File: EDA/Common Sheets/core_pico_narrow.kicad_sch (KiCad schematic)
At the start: 15 parts, among them J6 Conn_01x02, SW1 SW_DIP_x03, U1 Pico(2(W))

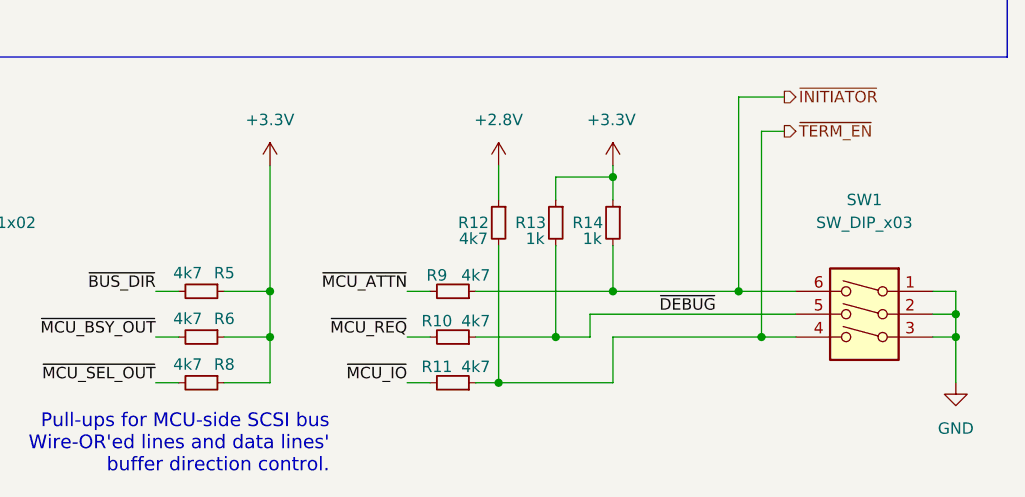
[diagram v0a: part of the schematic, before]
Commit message: Started work on thru-hole SCA wide variant
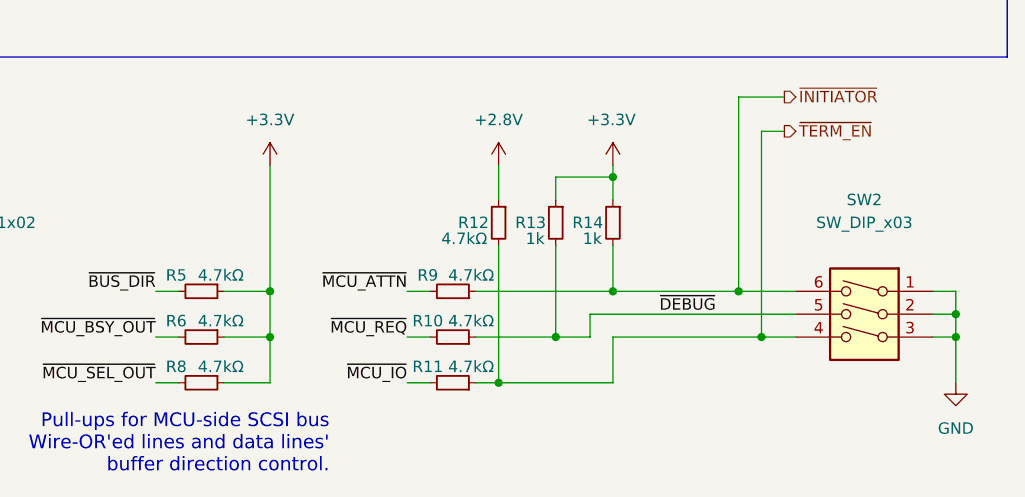
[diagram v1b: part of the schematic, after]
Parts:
- R10, R11, R12, R5, R6, R8, R9: value 4k7 -> 4.7kΩ
- renumbered SW1 to SW2
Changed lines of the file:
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@@
 		(dnp no)
 		(property "Reference" "R10"
-			(at 129.032 176.022 90)
-			(effects
-				(font
-					(size 1.27 1.27)
-				)
-			)
-		)
-		(property "Value" "4k7"
-			(at 133.35 176.022 90)
+			(at 128.016 176.022 90)
+			(effects
+				(font
+					(size 1.27 1.27)
+				)
+			)
+		)
+		(property "Value" "4.7kΩ"
+			(at 132.842 176.022 90)
 			(effects
 				(font
@@
 		(dnp no)
 		(property "Reference" "R6"
-			(at 105.41 175.768 90)
-			(effects
-				(font
-					(size 1.27 1.27)
-				)
-			)
-		)
-		(property "Value" "4k7"
-			(at 101.346 175.768 90)
+			(at 100.076 176.022 90)
+			(effects
+				(font
+					(size 1.27 1.27)
+				)
+			)
+		)
+		(property "Value" "4.7kΩ"
+			(at 105.029 176.022 90)
 			(effects
 				(font
@@
 		(dnp no)
 		(property "Reference" "R9"
-			(at 129.032 170.942 90)
-			(effects
-				(font
-					(size 1.27 1.27)
-				)
-			)
-		)
-		(property "Value" "4k7"
-			(at 133.35 170.942 90)
+			(at 128.016 170.942 90)
+			(effects
+				(font
+					(size 1.27 1.27)
+				)
+			)
+		)
+		(property "Value" "4.7kΩ"
+			(at 132.842 170.942 90)
 			(effects
 				(font
@@
 		(dnp no)
 		(property "Reference" "R8"
-			(at 105.41 180.848 90)
-			(effects
-				(font
-					(size 1.27 1.27)
-				)
-			)
-		)
-		(property "Value" "4k7"
-			(at 101.346 180.848 90)
+			(at 100.076 181.102 90)
+			(effects
+				(font
+					(size 1.27 1.27)
+				)
+			)
+		)
+		(property "Value" "4.7kΩ"
+			(at 105.029 181.102 90)
 			(effects
 				(font
@@
 		(dnp no)
 		(property "Reference" "R11"
-			(at 129.032 181.102 90)
-			(effects
-				(font
-					(size 1.27 1.27)
-				)
-			)
-		)
-		(property "Value" "4k7"
-			(at 133.35 181.102 90)
+			(at 128.016 181.102 90)
+			(effects
+				(font
+					(size 1.27 1.27)
+				)
+			)
+		)
+		(property "Value" "4.7kΩ"
+			(at 132.842 181.102 90)
 			(effects
 				(font
@@
 		(dnp no)
 		(property "Reference" "R5"
-			(at 105.41 170.688 90)
-			(effects
-				(font
-					(size 1.27 1.27)
-				)
-			)
-		)
-		(property "Value" "4k7"
-			(at 101.346 170.688 90)
+			(at 100.076 170.942 90)
+			(effects
+				(font
+					(size 1.27 1.27)
+				)
+			)
+		)
+		(property "Value" "4.7kΩ"
+			(at 105.029 170.942 90)
 			(effects
 				(font
@@
 			)
 		)
-		(property "Value" "4k7"
-			(at 133.096 166.878 0)
+		(property "Value" "4.7kΩ"
+			(at 132.08 166.878 0)
 			(effects
 				(font
@@
 		(on_board yes)
 		(dnp no)
-		(property "Reference" "SW1"
+		(property "Reference" "SW2"
 			(at 176.53 162.56 0)
 			(effects
@@
 			(project "GBSCSI2_2.5N_Pico"
 				(path "/93ed3756-682c-4bf3-aa83-42c6b59d82c2/871f9ffd-aa9f-4db2-af7f-735335bcb730"
-					(reference "SW1")
-					(unit 1)
-				)
+					(reference "SW2")
+					(unit 1)
+				)

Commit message: Resuming work
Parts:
- U1: footprint GBSCSI:RPi_Pico_W_SMD_TH -> GBSCSI:RPi_Pico_W_SMD
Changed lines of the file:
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@@
 		)
 		(instances
-			(project "GBSCSI2_2.5N_Pico"
+			(project "GBSCSI2_DB25_Pico"
 				(path "/93ed3756-682c-4bf3-aa83-42c6b59d82c2/871f9ffd-aa9f-4db2-af7f-735335bcb730"
 					(reference "D5")
@@
 		)
 		(instances
-			(project "GBSCSI2_2.5N_Pico"
+			(project "GBSCSI2_DB25_Pico"
 				(path "/93ed3756-682c-4bf3-aa83-42c6b59d82c2/871f9ffd-aa9f-4db2-af7f-735335bcb730"
 					(reference "R10")
@@
 		)
 		(instances
-			(project "GBSCSI2_2.5N_Pico"
+			(project "GBSCSI2_DB25_Pico"
 				(path "/93ed3756-682c-4bf3-aa83-42c6b59d82c2/871f9ffd-aa9f-4db2-af7f-735335bcb730"
 					(reference "#PWR02")
@@
 		)
 		(instances
-			(project "GBSCSI2_2.5N_Pico"
+			(project "GBSCSI2_DB25_Pico"
 				(path "/93ed3756-682c-4bf3-aa83-42c6b59d82c2/871f9ffd-aa9f-4db2-af7f-735335bcb730"
 					(reference "#PWR021")
@@
 		)
 		(instances
-			(project "GBSCSI2_2.5N_Pico"
+			(project "GBSCSI2_DB25_Pico"
 				(path "/93ed3756-682c-4bf3-aa83-42c6b59d82c2/871f9ffd-aa9f-4db2-af7f-735335bcb730"
 					(reference "#PWR03")
@@
 		)
 		(instances
-			(project "GBSCSI2_2.5N_Pico"
+			(project "GBSCSI2_DB25_Pico"
 				(path "/93ed3756-682c-4bf3-aa83-42c6b59d82c2/871f9ffd-aa9f-4db2-af7f-735335bcb730"
 					(reference "#PWR023")
@@
 		)
 		(instances
-			(project "GBSCSI2_2.5N_Pico"
+			(project "GBSCSI2_DB25_Pico"
 				(path "/93ed3756-682c-4bf3-aa83-42c6b59d82c2/871f9ffd-aa9f-4db2-af7f-735335bcb730"
 					(reference "R6")
@@
 		)
 		(instances
-			(project "GBSCSI2_2.5N_Pico"
+			(project "GBSCSI2_DB25_Pico"
 				(path "/93ed3756-682c-4bf3-aa83-42c6b59d82c2/871f9ffd-aa9f-4db2-af7f-735335bcb730"
 					(reference "R55")
@@
 		)
 		(instances
-			(project "GBSCSI2_2.5N_Pico"
+			(project "GBSCSI2_DB25_Pico"
 				(path "/93ed3756-682c-4bf3-aa83-42c6b59d82c2/871f9ffd-aa9f-4db2-af7f-735335bcb730"
 					(reference "R9")
@@
 		)
 		(instances
-			(project "GBSCSI2_2.5N_Pico"
+			(project "GBSCSI2_DB25_Pico"
 				(path "/93ed3756-682c-4bf3-aa83-42c6b59d82c2/871f9ffd-aa9f-4db2-af7f-735335bcb730"
 					(reference "#PWR04")
@@
 		)
 		(instances
-			(project "GBSCSI2_2.5N_Pico"
+			(project "GBSCSI2_DB25_Pico"
 				(path "/93ed3756-682c-4bf3-aa83-42c6b59d82c2/871f9ffd-aa9f-4db2-af7f-735335bcb730"
 					(reference "#PWR017")
@@
 		)
 		(instances
-			(project "GBSCSI2_2.5N_Pico"
+			(project "GBSCSI2_DB25_Pico"
 				(path "/93ed3756-682c-4bf3-aa83-42c6b59d82c2/871f9ffd-aa9f-4db2-af7f-735335bcb730"
 					(reference "#FLG05")
@@
 		)
 		(instances
-			(project "GBSCSI2_2.5N_Pico"
+			(project "GBSCSI2_DB25_Pico"
 				(path "/93ed3756-682c-4bf3-aa83-42c6b59d82c2/871f9ffd-aa9f-4db2-af7f-735335bcb730"
 					(reference "R13")
@@
 		)
 		(instances
-			(project "GBSCSI2_2.5N_Pico"
+			(project "GBSCSI2_DB25_Pico"
 				(path "/93ed3756-682c-4bf3-aa83-42c6b59d82c2/871f9ffd-aa9f-4db2-af7f-735335bcb730"
 					(reference "#PWR022")
@@
 		)
 		(instances
-			(project "GBSCSI2_2.5N_Pico"
+			(project "GBSCSI2_DB25_Pico"
 				(path "/93ed3756-682c-4bf3-aa83-42c6b59d82c2/871f9ffd-aa9f-4db2-af7f-735335bcb730"
 					(reference "R17")
@@
 		)
 		(instances
-			(project "GBSCSI2_2.5N_Pico"
+			(project "GBSCSI2_DB25_Pico"
 				(path "/93ed3756-682c-4bf3-aa83-42c6b59d82c2/871f9ffd-aa9f-4db2-af7f-735335bcb730"
 					(reference "R8")
@@
 		)
 		(instances
-			(project "GBSCSI2_2.5N_Pico"
+			(project "GBSCSI2_DB25_Pico"
 				(path "/93ed3756-682c-4bf3-aa83-42c6b59d82c2/871f9ffd-aa9f-4db2-af7f-735335bcb730"
 					(reference "#PWR01")
@@
 		)
 		(instances
-			(project "GBSCSI2_2.5N_Pico"
+			(project "GBSCSI2_DB25_Pico"
 				(path "/93ed3756-682c-4bf3-aa83-42c6b59d82c2/871f9ffd-aa9f-4db2-af7f-735335bcb730"
 					(reference "#PWR020")
@@
 		)
 		(instances
-			(project "GBSCSI2_2.5N_Pico"
+			(project "GBSCSI2_DB25_Pico"
 				(path "/93ed3756-682c-4bf3-aa83-42c6b59d82c2/871f9ffd-aa9f-4db2-af7f-735335bcb730"
 					(reference "#PWR024")
@@
 			)
 		)
-		(property "Footprint" "GBSCSI:RPi_Pico_W_SMD_TH"
+		(property "Footprint" "GBSCSI:RPi_Pico_W_SMD"
 			(at 102.87 76.2 90)
 			(effects
@@
 		)
 		(instances
-			(project "GBSCSI2_2.5N_Pico"
+			(project "GBSCSI2_DB25_Pico"
 				(path "/93ed3756-682c-4bf3-aa83-42c6b59d82c2/871f9ffd-aa9f-4db2-af7f-735335bcb730"
 					(reference "U1")
@@
 		)
 		(instances
-			(project "GBSCSI2_2.5N_Pico"
+			(project "GBSCSI2_DB25_Pico"
 				(path "/93ed3756-682c-4bf3-aa83-42c6b59d82c2/871f9ffd-aa9f-4db2-af7f-735335bcb730"
 					(reference "R11")
@@
 		)
 		(instances
-			(project "GBSCSI2_2.5N_Pico"
+			(project "GBSCSI2_DB25_Pico"
 				(path "/93ed3756-682c-4bf3-aa83-42c6b59d82c2/871f9ffd-aa9f-4db2-af7f-735335bcb730"
 					(reference "R5")
@@
 		)
 		(instances
-			(project "GBSCSI2_2.5N_Pico"
+			(project "GBSCSI2_DB25_Pico"
 				(path "/93ed3756-682c-4bf3-aa83-42c6b59d82c2/871f9ffd-aa9f-4db2-af7f-735335bcb730"
 					(reference "R12")
@@
 		)
 		(instances
-			(project "GBSCSI2_2.5N_Pico"
+			(project "GBSCSI2_DB25_Pico"
 				(path "/93ed3756-682c-4bf3-aa83-42c6b59d82c2/871f9ffd-aa9f-4db2-af7f-735335bcb730"
 					(reference "J6")
@@
 		)
 		(instances
-			(project "GBSCSI2_2.5N_Pico"
+			(project "GBSCSI2_DB25_Pico"
 				(path "/93ed3756-682c-4bf3-aa83-42c6b59d82c2/871f9ffd-aa9f-4db2-af7f-735335bcb730"
 					(reference "R14")
@@
 		)
 		(instances
-			(project "GBSCSI2_2.5N_Pico"
+			(project "GBSCSI2_DB25_Pico"
 				(path "/93ed3756-682c-4bf3-aa83-42c6b59d82c2/871f9ffd-aa9f-4db2-af7f-735335bcb730"
 					(reference "SW2")
@@
 		)
 		(instances
-			(project "GBSCSI2_2.5N_Pico"
+			(project "GBSCSI2_DB25_Pico"
 				(path "/93ed3756-682c-4bf3-aa83-42c6b59d82c2/871f9ffd-aa9f-4db2-af7f-735335bcb730"
 					(page "3")
